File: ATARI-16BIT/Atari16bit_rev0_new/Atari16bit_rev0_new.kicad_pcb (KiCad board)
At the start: 2 copper layers, 10 parts, among them J1 ACSI (IDC-20), J2 SD Card module, U1 74LS641, U2 74LS641, U3 74LS641, U4 ESP32-DevKitC

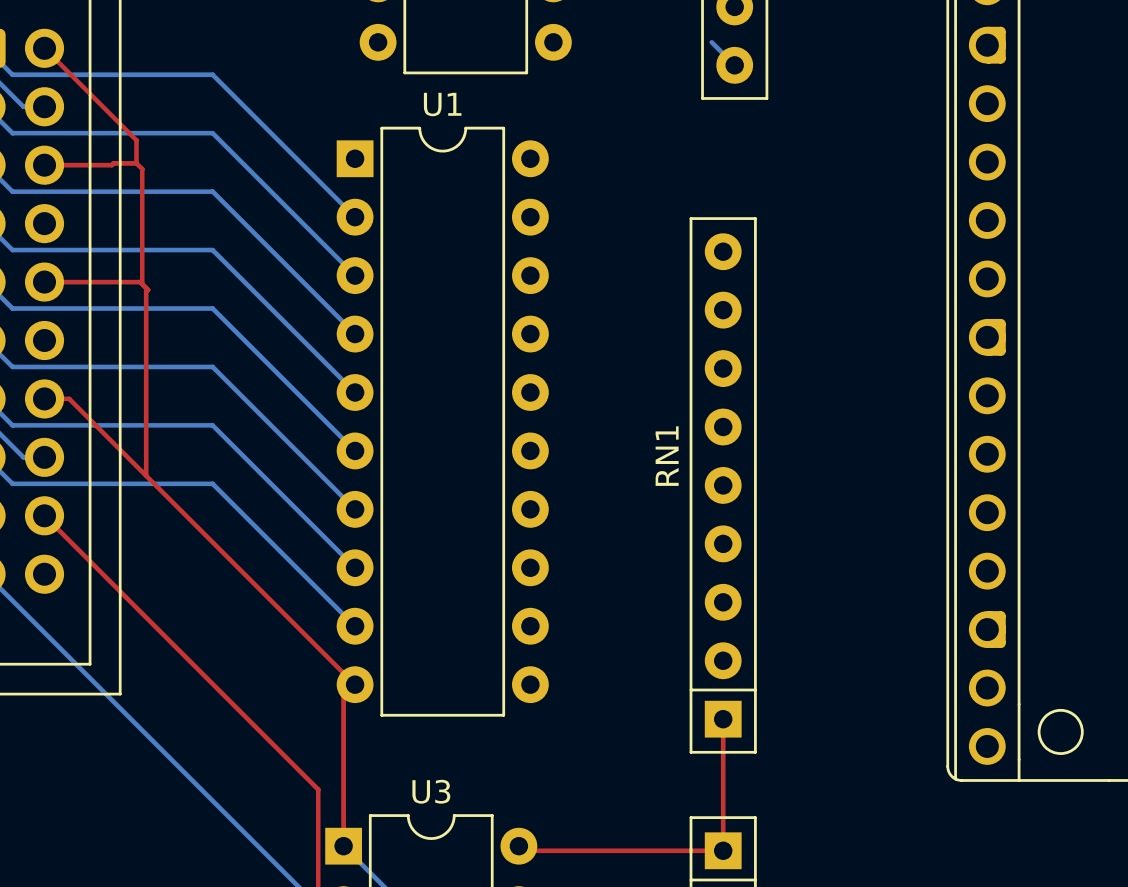
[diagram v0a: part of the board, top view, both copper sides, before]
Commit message: [Atari16bit] PCB update WIP
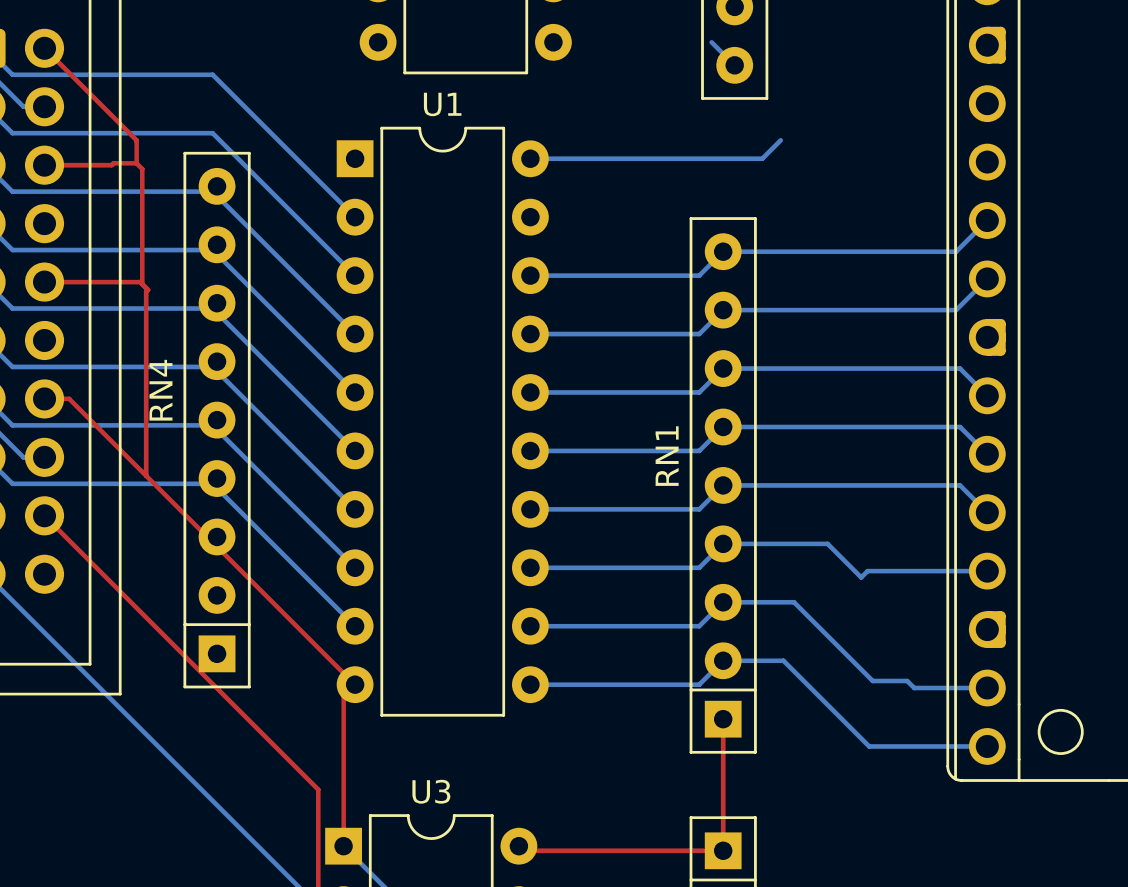
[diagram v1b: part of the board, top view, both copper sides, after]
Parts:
- added RN4: 10k, Resistor_THT:R_Array_SIP9, F.Cu at (84.5, 91.3)
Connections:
- A1 pad 10: unconnected-(A1-GPIO7-Pad10) -> DDIR
- A1 pad 5: unconnected-(A1-GPIO3-Pad5) -> Pico_DRQ
- A1 pad 6: Pico_DRQ -> ESP_UART_RX
- A1 pad 7: DDIR -> ESP_UART_TX
- U4 pad 27: unconnected-(U4-GPIO16-Pad27) -> ESP_UART_RX
- U4 pad 28: unconnected-(U4-GPIO17-Pad28) -> ESP_UART_TX
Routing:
- net Pico_D6: track 0.00 -> 21.8 mm
- net Pico_D7: track 0.00 -> 21.8 mm
- net Pico_D5: track 0.00 -> 21.0 mm
- net Pico_D1: track 0.00 -> 20.9 mm
- net Pico_D0: track 0.00 -> 20.9 mm
- net Pico_D4: track 0.00 -> 20.8 mm
- net Pico_D3: track 0.00 -> 20.8 mm
- net Pico_D2: track 0.00 -> 20.8 mm
- net +3.3V: track 14.7 -> 25.9 mm
